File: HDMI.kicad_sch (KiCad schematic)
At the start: 10 parts, among them IC6 TPS2553QDBVRQ1, J9 HDMI_E

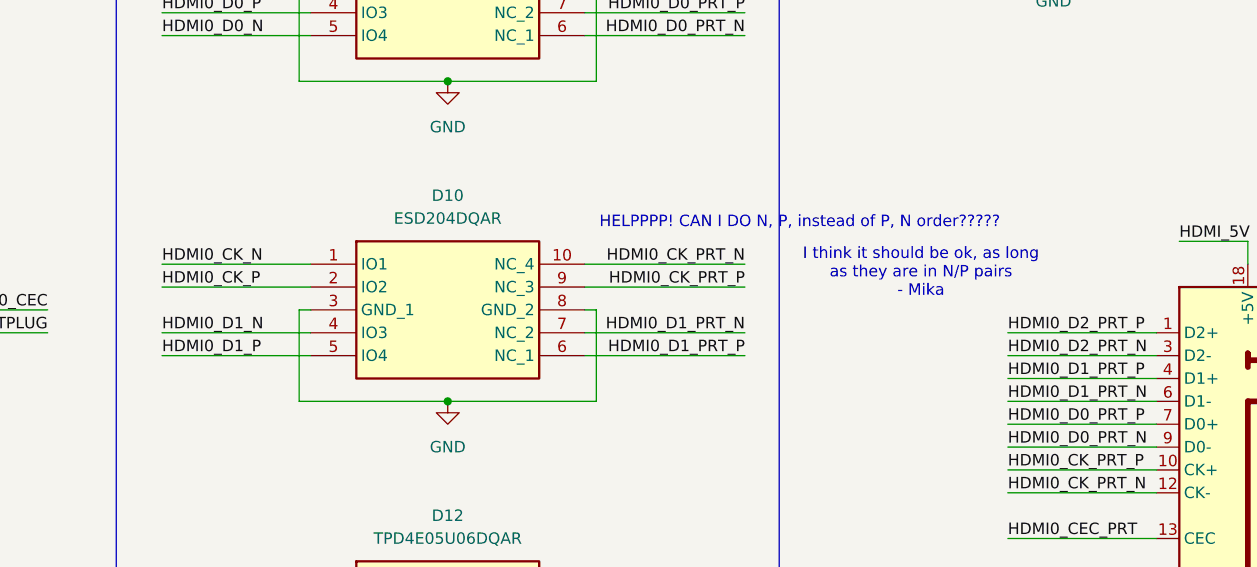
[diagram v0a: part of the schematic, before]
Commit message: Migrate to USB C and added some ESD protections on Vbus; might still have some issues
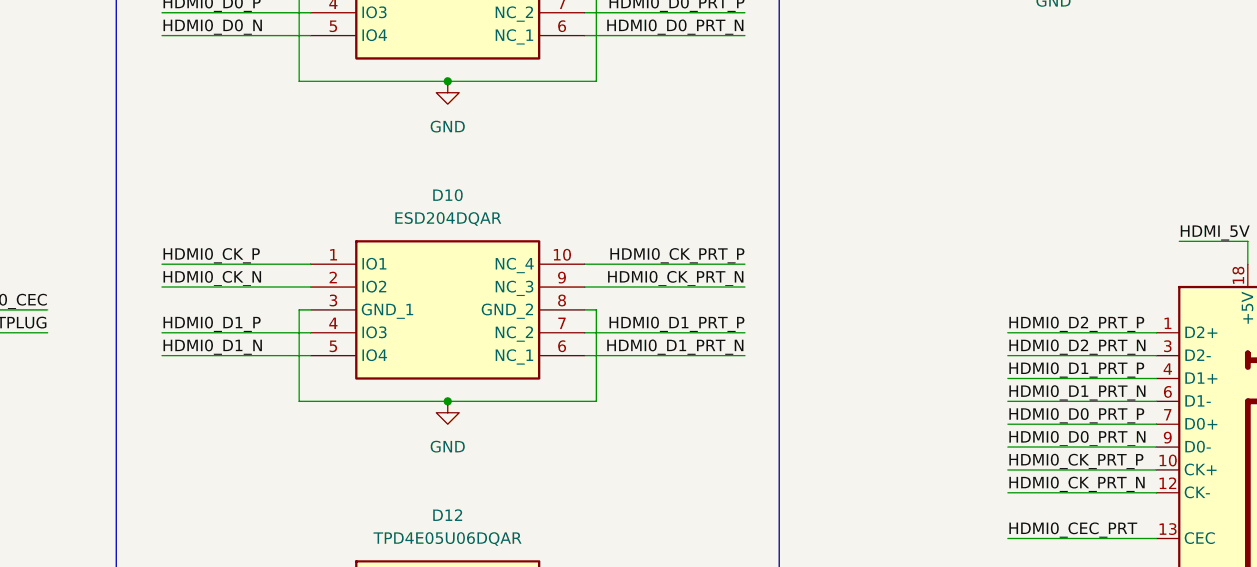
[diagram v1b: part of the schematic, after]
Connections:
- net HDMI0_CK_N: now also D10.2 (IO2); no longer D10.1 (IO1)
- net HDMI0_CK_P: now also D10.1 (IO1); no longer D10.2 (IO2)
- net HDMI0_CK_PRT_N: now also D10.9 (NC_3); no longer D10.10 (NC_4)
- net HDMI0_CK_PRT_P: now also D10.10 (NC_4); no longer D10.9 (NC_3)
- net HDMI0_D1_N: now also D10.5 (IO4); no longer D10.4 (IO3)
- net HDMI0_D1_P: now also D10.4 (IO3); no longer D10.5 (IO4)
- net HDMI0_D1_PRT_N: now also D10.6 (NC_1); no longer D10.7 (NC_2)
- net HDMI0_D1_PRT_P: now also D10.7 (NC_2); no longer D10.6 (NC_1)
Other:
- note removed: "HELPPPP! CAN I DO N, P, instead of P, N order?????"
- note removed: "I think it should be ok, as long as they are in N/P pairs - Mika"

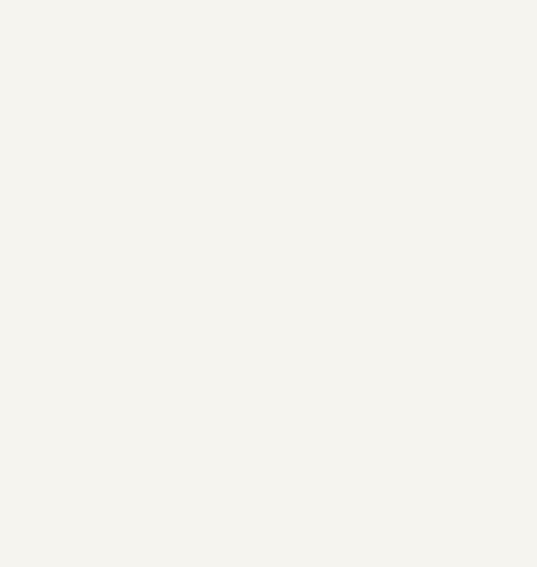
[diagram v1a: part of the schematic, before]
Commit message: fixed erc and removed old schematics
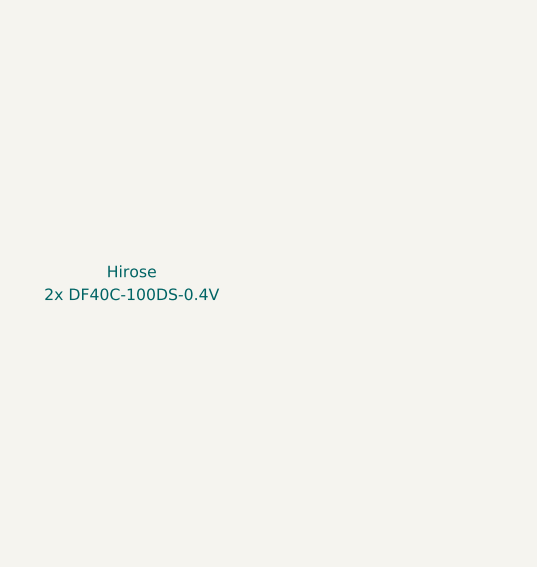
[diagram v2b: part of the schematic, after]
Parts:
- D10, D8: Arrow Part Number (none) -> ESD204DQAR; Arrow Price/Stock (none) -> https://www.arrow.com/en/products/esd204dqar/texas-instrume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; Height (none) -> 0.55; Manufacturer_Name (none) -> Texas Instruments; Manufacturer_Part_Number (none) -> ESD204DQAR; Mouser Part Number (none) -> 595-ESD204DQAR; Mouser Price/Stock (none) -> https://www.mouser.co.uk/ProductDetail/Texas-Instruments/ES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
- IC6: Arrow Part Number (none) -> TPS2553QDBVRQ1; Arrow Price/Stock (none) -> https://www.arrow.com/en/products/tps2553qdbvrq1/texas-inst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; Height (none) -> 1.45; Manufacturer_Name (none) -> Texas Instruments; Manufacturer_Part_Number (none) -> TPS2553QDBVRQ1; Mouser Part Number (none) -> 595-TPS2553QDBVRQ1; Mouser Price/Stock (none) -> https://www.mouser.co.uk/ProductDetail/Texas-Instruments/TP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
- Module1: Field4 (none) -> Hirose; Field5 (none) -> 2x DF40C-100DS-0.4V

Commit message: changed usb to be simpler (no inbuilt hub)
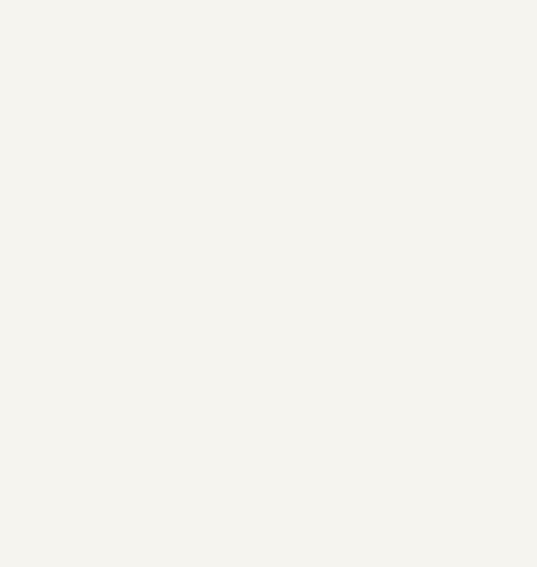
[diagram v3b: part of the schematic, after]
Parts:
- D10, D8: Arrow Part Number ESD204DQAR -> (none); Arrow Price/Stock https://www.arrow.com/en/products/esd204dqar/texas-instrume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 -> (none); Height 0.55 -> (none); Manufacturer_Name Texas Instruments -> (none); Manufacturer_Part_Number ESD204DQAR -> (none); Mouser Part Number 595-ESD204DQAR -> (none); Mouser Price/Stock https://www.mouser.co.uk/ProductDetail/Texas-Instruments/ES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 -> (none)
- D12: Arrow Part Number TPD4E05U06DQAR -> (none); Arrow Price/Stock https://www.arrow.com/en/products/tpd4e05u06dqar/texas-inst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 -> (none); Manufacturer_Name Texas Instruments -> (none); Manufacturer_Part_Number TPD4E05U06DQAR -> (none); Mouser Part Number 595-TPD4E05U06DQAR -> (none); Mouser Price/Stock https://www.mouser.co.uk/ProductDetail/Texas-Instruments/TP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 -> (none); P/N (none) -> TPD4E05U06DQAR
- IC6: Arrow Part Number TPS2553QDBVRQ1 -> (none); Arrow Price/Stock https://www.arrow.com/en/products/tps2553qdbvrq1/texas-inst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 -> (none); Height 1.45 -> (none); Manufacturer_Name Texas Instruments -> (none); Manufacturer_Part_Number TPS2553QDBVRQ1 -> (none); Mouser Part Number 595-TPS2553QDBVRQ1 -> (none); Mouser Price/Stock https://www.mouser.co.uk/ProductDetail/Texas-Instruments/TP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 -> (none)
- Module1: Field4 Hirose -> (none); Field5 2x DF40C-100DS-0.4V -> (none)

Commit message: moved everything to front & 0603'd stuff
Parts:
- C3, C43: footprint Capacitor_SMD:C_0805_2012Metric -> Capacitor_SMD:C_0603_1608Metric
- R27, R28: footprint Resistor_SMD:R_0805_2012Metric -> Resistor_SMD:R_0603_1608Metric
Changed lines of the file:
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@@
 			)
 		)
-		(property "Footprint" "Capacitor_SMD:C_0805_2012Metric"
+		(property "Footprint" "Capacitor_SMD:C_0603_1608Metric"
 			(at 232.1052 43.18 0)
 			(effects
@@
 			)
 		)
-		(property "Footprint" "Capacitor_SMD:C_0805_2012Metric"
+		(property "Footprint" "Capacitor_SMD:C_0603_1608Metric"
 			(at 229.5652 63.5 0)
 			(effects
@@
 			)
 		)
-		(property "Footprint" "Resistor_SMD:R_0805_2012Metric"
+		(property "Footprint" "Resistor_SMD:R_0603_1608Metric"
 			(at 222.25 56.388 90)
 			(effects
@@
 			)
 		)
-		(property "Footprint" "Resistor_SMD:R_0805_2012Metric"
+		(property "Footprint" "Resistor_SMD:R_0603_1608Metric"
 			(at 271.018 55.88 90)
 			(effects

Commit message: changed a bunch of stuff, still have work
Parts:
- added C29: 100uF, Capacitor_SMD:C_0805_2012Metric, symbol Device:C
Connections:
- net GND: now also C29.2
- net HDMI_5V: now also C29.1
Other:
- note added: "Added this"
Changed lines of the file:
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@@
+		)
+	)
+	(text "Added this"
+		(exclude_from_sim no)
+		(at 256.032 94.742 0)
+		(effects
+			(font
+				(size 1.27 1.27)
+			)
 		)
 	)
@@
 	)
 	(junction
+		(at 246.38 91.44)
+		(diameter 0)
+		(color 0 0 0 0)
+	)
+	(junction
 		(at 34.29 69.85)
 		(diameter 1.016)
@@
 	(wire
 		(pts
+			(xy 240.03 91.44) (xy 246.38 91.44)
+		)
+		(stroke
+			(width 0)
+			(type default)
+		)
+	)
+	(wire
+		(pts
 			(xy 97.79 105.41) (xy 116.84 105.41)
 		)
@@
 	(wire
 		(pts
-			(xy 250.19 95.25) (xy 250.19 97.79)
+			(xy 250.19 91.44) (xy 250.19 97.79)
 		)
 		(stroke
@@
 	(wire
 		(pts
-			(xy 250.19 95.25) (xy 242.57 95.25)
-		)
-		(stroke
-			(width 0)
-			(type default)
-		)
-	)
-	(wire
-		(pts
 			(xy 144.78 148.59) (xy 161.29 148.59)
 		)
@@
 	(wire
 		(pts
+			(xy 240.03 99.06) (xy 246.38 99.06)
+		)
+		(stroke
+			(width 0)
+			(type default)
+		)
+	)
+	(wire
+		(pts
 			(xy 34.29 138.43) (xy 34.29 146.05)
 		)
@@
 			(width 0)
 			(type solid)
+		)
+	)
+	(wire
+		(pts
+			(xy 246.38 91.44) (xy 250.19 91.44)
+		)
+		(stroke
+			(width 0)
+			(type default)
 		)
 	)
@@
 	)
 	(label "HDMI_5V"
-		(at 242.57 95.25 0)
-		(effects
-			(font
-				(size 1.27 1.27)
-			)
-			(justify left bottom)
+		(at 240.03 91.44 180)
+		(effects
+			(font
+				(size 1.27 1.27)
+			)
+			(justify right bottom)
 		)
 	)
@@
 			)
 			(justify left)
+		)
+	)
+	(symbol
+		(lib_id "power:GND")
+		(at 240.03 99.06 0)
+		(unit 1)
+		(exclude_from_sim no)
+		(in_bom yes)
+		(on_board yes)
+		(dnp no)
+		(property "Reference" "#PWR041"
+			(at 240.03 105.41 0)
+			(effects
+				(font
+					(size 1.27 1.27)
+				)
+				(hide yes)
+			)
+		)
+		(property "Value" "GND"
+			(at 237.744 99.314 0)
+			(effects
+				(font
+					(size 1.27 1.27)
+				)
+			)
+		)
+		(property "Footprint" ""
+			(at 240.03 99.06 0)
+			(effects
+				(font
+					(size 1.27 1.27)
+				)
+				(hide yes)
+			)
+		)
+		(property "Datasheet" ""
+			(at 240.03 99.06 0)
+			(effects
+				(font
+					(size 1.27 1.27)
+				)
+				(hide yes)
+			)
+		)
+		(property "Description" "Power symbol creates a global label with name \"GND\" , ground"
+			(at 240.03 99.06 0)
+			(effects
+				(font
+					(size 1.27 1.27)
+				)
+				(hide yes)
+			)
+		)
+		(pin "1"
+		)
+		(instances
+			(project "PiBoard"
+				(path "/e4d65698-b8ec-4bf6-9f2b-a5010377155a/2dec5fd6-8756-425d-9ae9-2f1c2fc4e6c1"
+					(reference "#PWR041")
+					(unit 1)
+				)
+			)
 		)
 	)
@@
 					(unit 1)
 				)
+			)
+		)
+	)
+	(symbol
+		(lib_id "Device:C")
+		(at 246.38 95.25 0)
+		(unit 1)
+		(exclude_from_sim no)
+		(in_bom yes)
+		(on_board yes)
+		(dnp no)
+		(property "Reference" "C29"
+			(at 237.49 93.9546 0)
+			(effects
+				(font
+					(size 1.27 1.27)
+				)
+				(justify left)
+			)
+		)
+		(property "Value" "100uF"
+			(at 237.49 96.266 0)
+			(effects
+				(font
+					(size 1.27 1.27)
+				)
+				(justify left)
+			)
+		)
+		(property "Footprint" "Capacitor_SMD:C_0805_2012Metric"
+			(at 247.3452 99.06 0)
+			(effects
+				(font
+					(size 1.27 1.27)
+				)
+				(hide yes)
+			)
+		)
+		(property "Datasheet" "https://content.kemet.com/datasheets/KEM_C1002_X7R_SMD.pdf"
+			(at 246.38 95.25 0)
+			(effects
+				(font
+					(size 1.27 1.27)
+				)
+				(hide yes)
+			)
+		)
+		(property "Description" "Unpolarized capacitor"
+			(at 246.38 95.25 0)
+			(effects
+				(font
+					(size 1.27 1.27)
+				)
+				(hide yes)
+			)
+		)
+		(property "P/N" "C0805C104M5RACTU"
+			(at 246.38 95.25 0)
+			(effects
+				(font
+					(size 1.27 1.27)
+				)
+				(hide yes)
+			)
+		)
+		(pin "1"
+		)
+		(pin "2"
+		)
+		(instances
+			(project "PiBoard"
+				(path "/e4d65698-b8ec-4bf6-9f2b-a5010377155a/2dec5fd6-8756-425d-9ae9-2f1c2fc4e6c1"
+					(reference "C29")
+					(unit 1)
+				)

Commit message: my life is horrible
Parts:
- removed D10, D8: ESD204DQAR, Controls_Pi:ESD204DQAR, symbol ESD204DQAR:ESD204DQAR
- removed Module1: ComputeModule4-CM4, CM4IO:Raspberry-Pi-4-Compute-Module, symbol CM4IO:ComputeModule4-CM4
- added C13, C16, C17, C20, C21, C28, C32, C33: 100n, Capacitor_SMD:C_0603_1608Metric, symbol Device:C
- added C14: 10uF, Capacitor_SMD:C_0603_1608Metric, symbol Device:C
- added C15: 120uF, Capacitor_SMD:C_0603_1608Metric, symbol Device:C
- added D10, D11, D15, D17, D18, D3, D8: TPD4E05U06DQAR, Controls_Pi:DQA_R-PUSON-N10_, symbol TPD4E05U06DQAR:TPD4E05U06DQAR
- added D6: VBUS_PWR LED, LED_SMD:LED_0603_1608Metric, symbol Device:LED
- added FB3, FB4, FB5: FerriteBead, Inductor_SMD:L_1206_3216Metric, symbol Device:FerriteBead
- added IC5, IC8, IC9: TPS2557QDRBTQ1, SON65P300X300X100-9N-D, symbol TPS2557QDRBTQ1:TPS2557QDRBTQ1
- added J13: USB_C_Receptacle_USB2.0_16P, Connector_USB:USB_C_Receptacle_GCT_USB4105-xx-A_16P_TopMnt_Horizontal, symbol Connector:USB_C_Receptacle_USB2.0_16P
- added J15, J7: USB_C_Receptacle, symbol Connector:USB_C_Receptacle
- added Module2: ComputeModule5-CM5, CM5IO:Raspberry-Pi-5-Compute-Module, symbol CM5IO:ComputeModule5-CM5
- added R11, R12, R16, R21: 56k, Resistor_SMD:R_0603_1608Metric, symbol Device:R
- added R18: 1.5k, Resistor_SMD:R_0603_1608Metric, symbol Device:R
- added R22, R26: 100k, Resistor_SMD:R_0603_1608Metric, symbol Device:R
- added R23, R29: 120k, Resistor_SMD:R_0603_1608Metric, symbol Device:R
- added R41: 20k, Resistor_SMD:R_0603_1608Metric, symbol Device:R
- R27: value 100n -> 100k
- R28: value 82k -> 56k
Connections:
- net HDMI0_CK_PRT_N is gone; now on net HDMI0_CK_N: J9.12 (CK-)
- net HDMI0_CK_PRT_P is gone; now on net HDMI0_CK_P: J9.10 (CK+)
- net HDMI0_D0_PRT_N is gone; now on net HDMI0_D0_N: J9.9 (D0-)
- net HDMI0_D0_PRT_P is gone; now on net HDMI0_D0_P: J9.7 (D0+)
- net HDMI0_D1_PRT_N is gone; now on net HDMI0_D1_N: J9.6 (D1-)
- net HDMI0_D1_PRT_P is gone; now on net HDMI0_D1_P: J9.4 (D1+)
- net HDMI0_D2_PRT_N is gone; now on net HDMI0_D2_N: J9.3 (D2-)
- net HDMI0_D2_PRT_P is gone; now on net HDMI0_D2_P: J9.1 (D2+)
- net GLOBAL_EN: now also R22.2, R26.2
- net GND: now also C13.2, C14.2, C15.2, C16.2, C17.2, C20.2, C21.2, C28.2, C32.2, C33.2, D10.3 (GND_1), D10.8 (GND_2), D11.3 (GND_1), D11.8 (GND_2), D15.3 (GND_1), D15.8 (GND_2), D17.3 (GND_1), D17.8 (GND_2), D18.3 (GND_1), D18.8 (GND_2), D3.3 (GND_1), D3.8 (GND_2), D6.1 (K), D8.3 (GND_1), D8.8 (GND_2), IC5.1 (GND), IC5.9 (EP), IC8.1 (GND), IC8.9 (EP), IC9.1 (GND), IC9.9 (EP), J13.A1 (GND), J13.A12 (GND), J13.B1 (GND), J13.B12 (GND), J13.S1 (SHIELD), J15.A1 (GND), J15.A12 (GND), J15.B1 (GND), J15.B12 (GND), J15.S1 (SHIELD), J7.A1 (GND), J7.A12 (GND), J7.B1 (GND), J7.B12 (GND), J7.S1 (SHIELD), Module2.107 (GND), Module2.108 (GND), Module2.113 (GND), Module2.114 (GND), Module2.119 (GND), Module2.120 (GND), Module2.125 (GND), Module2.126 (GND), Module2.131 (GND), Module2.132 (GND), Module2.137 (GND), Module2.138 (GND), Module2.144 (GND), Module2.150 (GND), Module2.155 (GND), Module2.156 (GND), Module2.161 (GND), Module2.162 (GND), Module2.167 (GND), Module2.168 (GND), Module2.173 (GND), Module2.174 (GND), Module2.179 (GND), Module2.180 (GND), Module2.185 (GND), Module2.186 (GND), Module2.191 (GND), Module2.192 (GND), Module2.197 (GND), Module2.198 (GND), R11.2, R12.1, R23.2, R29.2, R41.2
- net HDMI0_CEC: now also J9.13 (CEC), D3.1 (D1+), D3.10 (NC_4), Module2.151 (HDMI0_CEC); no longer D12.1 (D1+)
- net HDMI0_CK_N: now also D12.2 (D1-), D12.9 (NC_3), Module2.190 (HDMI0_CLK_N)
- net HDMI0_CK_P: now also D12.1 (D1+), D12.10 (NC_4), Module2.188 (HDMI0_CLK_P)
- net HDMI0_D0_N: now also D8.5 (D2-), D8.6 (NC_1), Module2.184 (HDMI0_TX0_N)
- net HDMI0_D0_P: now also D8.4 (D2+), D8.7 (NC_2), Module2.182 (HDMI0_TX0_P)
- net HDMI0_D1_N: now also D12.5 (D2-), D12.6 (NC_1), Module2.178 (HDMI0_TX1_N)
- net HDMI0_D1_P: now also D12.4 (D2+), D12.7 (NC_2), Module2.176 (HDMI0_TX1_P)
- net HDMI0_D2_N: now also D8.2 (D1-), D8.9 (NC_3), Module2.172 (HDMI0_TX2_N)
- net HDMI0_D2_P: now also D8.1 (D1+), D8.10 (NC_4), Module2.170 (HDMI0_TX2_P)
- net HDMI0_HOTPLUG: now also Module2.153 (HDMI0_HOTPLUG)
- net HDMI0_SCL: now also J9.15 (SCL), D3.4 (D2+), D3.7 (NC_2), Module2.200 (HDMI0_SCL); no longer D12.4 (D2+)
- net HDMI0_SDA: now also J9.16 (SDA), D3.5 (D2-), D3.6 (NC_1), Module2.199 (HDMI0_SDA); no longer D12.5 (D2-)
- net +5V_PWR renamed +5V
- net +5V: now also C17.1, C28.1, C33.1, IC5.6 (OUT_1), IC8.6 (OUT_1), IC9.6 (OUT_1), R16.2, R21.2
- removed net HDMI0_CEC_PRT: D12.10 (NC_4), J9.13 (CEC)
- removed net HDMI0_SCL_PRT: D12.6 (NC_1), J9.15 (SCL)
- removed net HDMI0_SDA_PRT: D12.7 (NC_2), J9.16 (SDA)
- new net: C13.1, C14.1, FB4.1, J15.A4 (VBUS), J15.A9 (VBUS), J15.B4 (VBUS), J15.B9 (VBUS)
- new net: C15.1, C16.1, FB5.1, J7.A4 (VBUS), J7.A9 (VBUS), J7.B4 (VBUS), J7.B9 (VBUS)
- new net: J7.A5 (CC1), R16.1
- new net: J7.B5 (CC2), R21.1
- new net: IC5.4 (EN), R22.1
- new net: IC5.5 (ILIM), R23.1
- new net: C21.1, FB3.2, J13.A4 (VBUS), J13.A9 (VBUS), J13.B4 (VBUS), J13.B9 (VBUS)
- new net: IC9.5 (ILIM), R41.1
- new net: IC8.4 (EN), R26.1
- new net: IC8.5 (ILIM), R29.1
- new net: D6.2 (A), R18.2
- new net: J15.B5 (CC2), R12.2
- new net: J15.A5 (CC1), R11.1
- new net CC1: D17.1 (D1+), D17.10 (NC_4), J13.A5 (CC1)
- new net CC2: D17.2 (D1-), D17.9 (NC_3), J13.B5 (CC2)
- new net USB_DBG_D+: D10.2 (D1-), D10.9 (NC_3), J15.A6 (D+), J15.B6 (D+), Module2.163 (USB3-1-D_P)
- new net USB_DBG_D-: D10.1 (D1+), D10.10 (NC_4), J15.A7 (D-), J15.B7 (D-), Module2.165 (USB3-1-D_N)
- new net USB_DBG_RX1+: D11.2 (D1-), D11.9 (NC_3), J15.B11 (RX1+), Module2.159 (USB3-1-RX_P)
- new net USB_DBG_RX1-: D11.1 (D1+), D11.10 (NC_4), J15.B10 (RX1-), Module2.157 (USB3-1-RX_N)
- new net USB_DBG_TX1+: D11.5 (D2-), D11.6 (NC_1), J15.A2 (TX1+), Module2.171 (USB3-1-TX_P)
- new net USB_DBG_TX1-: D11.4 (D2+), D11.7 (NC_2), J15.A3 (TX1-), Module2.169 (USB3-1-TX_N)
- new net USB_HUB_D+: D15.2 (D1-), D15.9 (NC_3), J7.A6 (D+), J7.B6 (D+), Module2.134 (USB3-0-D_P)
- new net USB_HUB_D-: D15.1 (D1+), D15.10 (NC_4), J7.A7 (D-), J7.B7 (D-), Module2.136 (USB3-0-D_N)
- new net USB_HUB_RX1+: D18.2 (D1-), D18.9 (NC_3), J7.B11 (RX1+), Module2.130 (USB3-0-RX_P)
- new net USB_HUB_RX1-: D18.1 (D1+), D18.10 (NC_4), J7.B10 (RX1-), Module2.128 (USB3-0-RX_N)
- new net USB_HUB_TX1+: D18.5 (D2-), D18.6 (NC_1), J7.A2 (TX1+), Module2.142 (USB3-0-TX_P)
- new net USB_HUB_TX1-: D18.4 (D2+), D18.7 (NC_2), J7.A3 (TX1-), Module2.140 (USB3-0-TX_N)
- new net USB_OTG: Module2.101 (USB_OTG_ID)
- new net USB_PWR_D+: D17.5 (D2-), D17.6 (NC_1), J13.A6 (D+), J13.B6 (D+), Module2.105 (USB2_P)
- new net USB_PWR_D-: D17.4 (D2+), D17.7 (NC_2), J13.A7 (D-), J13.B7 (D-), Module2.103 (USB2_N)
- new net VBUS_DBG: C20.1, FB4.2, IC5.2 (IN_1)
- new net VBUS_Hub: C32.1, FB5.2, IC8.2 (IN_1)
- new net VBUS_PWR: FB3.1, IC9.2 (IN_1), IC9.4 (EN), R18.1
- no-connect marks 58 -> 76
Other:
- note added: "CM5 negotiates pwr thru CC1/2"
- note added: "DBG"
- note added: "ESD"
- note added: "HDMI"
- note added: "HUB"
- note added: "High speed pins"
- note added: "Ilim: ~5A"
- note added: "Ilim: ~900mA"
- note added: "Limit at ~500 mA"
- note added: "PWR"
- note added: "Set so that USB can provide 5V/5A to pi"
- note added: "Sink?"
- note added: "THIS NEEDS A FULL REVIEW"
- note added: "USB C Power Port"
- note added: "USB_OTG needs to be pulled low when connected to debug Pull high otherwise"
- note added: "USB_OTG needs to be pulled low when connected to debug Pull high otherwise (???)"
- note added: "VBUS -> 5V"
- note removed: "Limit at 300-350 mA"
- moved on the sheet: C29, C3, C43, D12, IC6, J9, R27, R28

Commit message: moved things to their own sheets
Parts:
- removed C13, C17, C20, C3, C43: 100n, Capacitor_SMD:C_0603_1608Metric, symbol Device:C
- removed C14: 10uF, Capacitor_SMD:C_0603_1608Metric, symbol Device:C
- removed C29: 100uF, Capacitor_SMD:C_0805_2012Metric, symbol Device:C
- removed D10, D11, D12, D3, D8: TPD4E05U06DQAR, Controls_Pi:DQA_R-PUSON-N10_, symbol TPD4E05U06DQAR:TPD4E05U06DQAR
- removed FB4: FerriteBead, Inductor_SMD:L_1206_3216Metric, symbol Device:FerriteBead
- removed IC5: TPS2557QDRBTQ1, SON65P300X300X100-9N-D, symbol TPS2557QDRBTQ1:TPS2557QDRBTQ1
- removed IC6: TPS2553QDBVRQ1, Controls_Pi:SOT95P280X145-6N, symbol TPS2553QDBVRQ1:TPS2553QDBVRQ1
- removed J15: USB_C_Receptacle, symbol Connector:USB_C_Receptacle
- removed J9: HDMI_E, Controls_Pi:MX50019NQ1, symbol Connector:HDMI_E
- removed R11, R12, R28: 56k, Resistor_SMD:R_0603_1608Metric, symbol Device:R
- removed R22, R27: 100k, Resistor_SMD:R_0603_1608Metric, symbol Device:R
- removed R23: 120k, Resistor_SMD:R_0603_1608Metric, symbol Device:R
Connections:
- no-connect marks 76 -> 60
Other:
- added sheet all_usb (all_usb.kicad_sch)
- added sheet hdmi_protected (hdmi_protected.kicad_sch)
- note removed: "Added this"
- note removed: "DBG"
- note removed: "ESD Protection Diodes for HDMI"
- note removed: "HDMI"
- note removed: "Limit at ~500 mA"
- note removed: "Pinout for ESD diodes configured for easy layout"
- note removed: "Sink?"
- note removed: "THIS NEEDS A FULL REVIEW"
- note removed: "USB_OTG needs to be pulled low when connected to debug Pull high otherwise (???)"
